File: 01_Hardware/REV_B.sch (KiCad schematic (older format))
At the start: 87 parts, among them J1 RaspberryPi, J10 Conn_01x03, J11 Conn_01x03, J12 Conn_01x03, J13 Conn_01x08, J14 Conn_01x01, J2 Conn_01x02, J3 Conn_01x02, J4 Conn_01x02, J5 Conn_01x08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

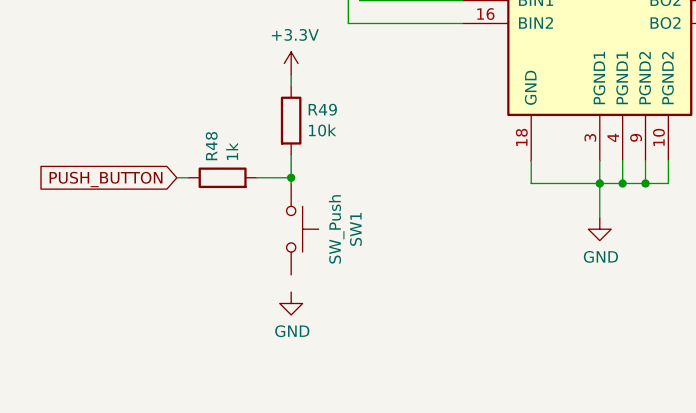
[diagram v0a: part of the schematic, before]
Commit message: Fix missing GND connection to PushButton
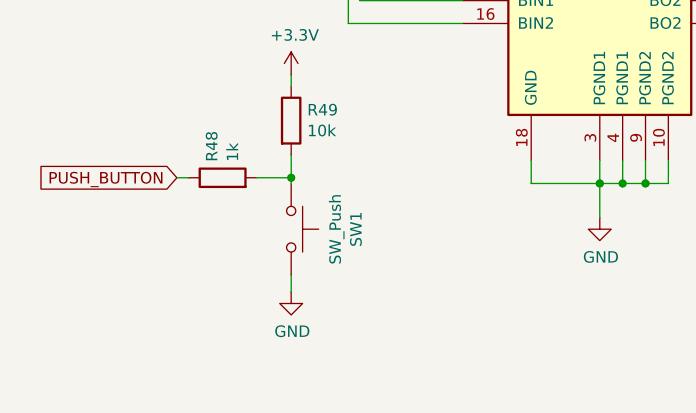
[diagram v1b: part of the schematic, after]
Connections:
- net GND: now also SW1.2
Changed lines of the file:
@@
 	1800 6825 1800 6725
 Connection ~ 1800 6825
+Wire Wire Line
+	1800 7250 1800 7325
 $EndSCHEMATC
